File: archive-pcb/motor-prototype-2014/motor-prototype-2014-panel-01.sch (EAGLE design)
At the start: 32 parts, among them J1 JST_VH_2RA, J2 MINIFITJR_HDR_2X2, J3 52852-0870, Q1 SIR438DP, Q2 SIR438DP, Q3 SIR438DP, Q4 SIR438DP, Q5 SIR438DP, Q6 SIR438DP, U1 IRS2336DSOIC28W

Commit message: finalized gerbers for lots of the working designs and moved them to archived directory
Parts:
- added A6-SEL, VSSSEL: (no value), jumper:SJ2W
- added C1, C3: 1 µF, rcl:C-USC0603
- added C10, C9: 1 nF, rcl:C-USC0402
- added C11: 22 µF, 16V, rcl:C-USC0402
- added C12: 100uF, SparkFun-Capacitors:100UF-63V-20%(ELECT)
- added C13: 0.47 µF, 16V, rcl:C-USC0402
- added C14, C15: 0.022 µF, 16V, rcl:C-USC0402
- added C16: 0.1 µF, 50V, rcl:C-USC0603
- added C17, C18: 2.2 µF, 50V, rcl:C-USC0603
- added C19: RC_CAPHE, RoboJackets-Capacitors:RC_CAPHE
- added C2: 2.2 µF, rcl:C-USC0603
- added C20: 0.1uF, adafruit:C-USC0805K
- added C4: 22 nF, rcl:C-USC1206
- added C5: 0.1 µf, rcl:C-USC0603
- added C6, C7, C8: 0.1 µF, rcl:C-USC0402
- added D1, D11, D16, D2, D3, D4, D5, D6, D7, D8, D9: RED, SparkFun-LED:LED-RED0603
- added D10: GRN, SparkFun-LED:LED-RED0603
- added D12, D13, D15: 1N4148WX, RoboJackets-Diodes:1N4148WX
- added D14: DFLS160-7, RoboJackets-Diodes:DFLS160-7
- added D17: P6SMB22A, RoboJackets-Diodes-bad:P6SMB22A
- added D18: MBRX160-TP, RoboJackets-Diodes:DIODE-SOD123
- added F2: FUSE1206, RoboJackets-ICs:FUSE1206
- added F3: FUSE, RoboJackets-Passive:FUSE
- added F4: FUSENANO2, RoboJackets-Passive:FUSENANO2
- added H1, U$4: MOUNTING_HOLE, RoboJackets-Passive:MOUNTING_HOLE
- added IC1: MCP23017, RoboJackets-ICs:MCP23017
- added IC2: DRV8302, RoboJackets-PowerICs:DRV8302
- added IC3: LM25010, RoboJackets-PowerICs:LM25010
- added IC4: MAX6675, adafruit:MAX6675
- added J4: XT-60, RoboJackets-Connectors:XT-60
- added J5: B2PS-VH(LF)(SN), RoboJackets-Connectors:B2PS-VH(LF)(SN)
- added JP1: (no value), SparkFun-Connectors:PINHD-2X10
- added JP2: (no value), SparkFun-Connectors:M03PTH
- added JP3: M02PTH, SparkFun-Connectors:M02PTH
- added JP4: Relay Signal, pinhead:PINHD-1X2/90
- added JP5: 5VIN, pinhead:PINHD-1X2/90
- added JP6: (no value), adafruit:PINHD-1X18
- added L1: SRR1280-101M, RoboJackets-Inductors:SRR1280-101M
- added LED: RGB Led Common Anode, pinhead:PINHD-1X4
- added PL1: (no value), con-molex-2:555X-8V
- added Q7, Q9: BJT-PNP_, RoboJackets-Discrete:BJT-PNP_
- added Q8: MMBT2222A-TP, RoboJackets-Discrete:MMBT2222A-TP
- added R10, R11, R12, R13, R6, R7, R8, R9: 330, SparkFun-Resistors:330OHM1/10W1%(0603)
- added R14, R35, R36, R38: 1 kΩ, rcl:R-US_R0402
- added R15: 150 kΩ, rcl:R-US_R0603
- added R16: 470 kΩ, rcl:R-US_R0402
- added R17: 6.8 kΩ, rcl:R-US_R0402
- added R18, R19: 10 kΩ, rcl:R-US_R0402
- added R20: 1 MΩ, rcl:R-US_R0402
- added R21, R22, R23, R24, R25, R26: 100 Ω, rcl:R-US_R0402
- added R27, R28: 0.002 Ω, rcl:R-US_R1206
- added R29, R30: 1.0 kΩ, rcl:R-US_R0402
- added R31: 1.5 Ω, rcl:R-US_R0402
- added R32: 200 kΩ, rcl:R-US_R0402
- added R33: 680 Ω, rcl:R-US_R0402
- added R34, R37: 100 kΩ, rcl:R-US_R0402
- added R39: 60, resistor:R-US_M0805
- added R40: (no value), resistor:R-US_R0805
- added RST, SERIAL: 22-23-2021, con-molex:22-23-2021
- added S1: SWS003, smd-special:SWS003
- added S2: (no value), RoboJackets-Switches:34EWMSP12MRT
- added S3: 1-1415899-3, RoboJackets-Switches:1-1415899-3
- added SJ1: JUMPER-PAD-3-2OF3_NC_BY_TRACE, SparkFun-Passives:JUMPER-PAD-3-2OF3_NC_BY_TRACE
- added SJ2, SJ3, SJ4, SJ5: JUMPER-PAD-2-NC_BY_TRACE, SparkFun-Passives:JUMPER-PAD-2-NC_BY_TRACE
- added SP1: Speaker, adafruit:SPEAKER/PS12
- added TCOUPLE: 1X2-3.5MM, adafruit:1X2-3.5MM
- added U$2: M18_, SparkFun-Connectors:M18_
- added U$7: ANANO3.3, ArduinoNano:ANANO3.3
- added U2, U3, U4: FDMS3606AS, RoboJackets-Discrete:FDMS3606AS
- added VOLTREG: (no value), RoboJackets-ICs:78MXXS
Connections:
- new net !FAULT!: IC2.!FAULT!, R14.2
- new net +3V3: D9.A, JP1.10, R18.1, S1.5, SJ1.1
- new net +5V: D10.A, D13.C, L1.P$1, R29.2, R31.2, S2.OFF, S3.2
- new net 15: JP6.15
- new net 16: JP6.16
- new net 4.5-18V: PL1-3.S
- new net A0: IC1.A0, R39.1, U$2.18, U$7.A0
- new net A1: IC1.A1, U$2.17
- new net A2: IC1.A2, U$2.16
- new net A5: LED.4, U$7.A5
- new net A6: A6-SEL.2, U$7.A6
- new net A7: LED.1, U$7.A7
- new net ADC_REF: IC2.REF, JP1.13
- new net BACKLIGHT: JP6.10, U$7.D9
- new net BATT+: F2.2, F3.2, F4.2, J4.1, SJ3.2, SJ5.2
- new net BATT_PROTECT_LOGIC: C16.1, C17.1, C18.1, D18.C, IC3.VIN, R32.2
- new net BATT_PROTECT_MOTOR: D17.C, F3.1, F4.1, S3.3, SJ2.2
- new net BIAS: IC2.BIAS, R20.1
- new net BOB: D18.A, F2.1, SJ4.2
- new net BST_A: C6.1, IC2.BST_A
- new net BST_B: C7.1, IC2.BST_B
- new net BST_C: C8.1, IC2.BST_C
- new net CARDDET: A6-SEL.3, JP6.18
- new net CP1: C4.1, IC2.CP1
- new net CP2: C4.2, IC2.CP2
- new net D/C: JP6.8, U$7.D8
- new net DC_CAL: IC2.DC_CAL, JP1.15
- new net DO: IC4.DO, U$7.D4
- new net DTC: IC2.DTC, R15.2, S1.6
- new net GH_A: IC2.GH_A, R26.1
- new net GH_A_F: R26.2, U2.G1
- new net GH_B: IC2.GH_B, R23.1
- new net GH_B_F: R23.2, U3.G1
- new net GH_C: IC2.GH_C, R22.1
- new net GH_C_F: R22.2, U4.G1
- new net GL_A: IC2.GL_A, R25.1
- new net GL_A_F: R25.2, U2.G2
- new net GL_B: IC2.GL_B, R24.1
- new net GL_B_F: R24.2, U3.G2
- new net GL_C: R21.2, U4.G2
- new net GPA0: IC1.GPA0, U$2.12
- new net GPA1: IC1.GPA1, U$2.11
- new net GPA2: IC1.GPA2, U$2.10
- new net GPA3: IC1.GPA3, U$2.9
- new net GPA4: IC1.GPA4, U$2.8
- new net GPA5: IC1.GPA5, U$2.7
- new net GPA6: IC1.GPA6, U$2.6
- new net GPA7: IC1.GPA7, U$2.5
- new net GPB0: IC1.GPB0, R6.2
- new net GPB1: IC1.GPB1, R7.2
- new net GPB2: IC1.GPB2, R8.2
- new net GPB3: IC1.GPB3, R9.2
- new net GPB4: IC1.GPB4, R10.2
- new net GPB5: IC1.GPB5, R11.2
- new net GPB6: IC1.GPB6, R12.2
- new net GPB7: IC1.GPB7, R13.2
- new net HALL-1.1: JP1.6, PL1-1.S
- new net HALL-1.2: JP1.4, PL1-2.S
- new net HALL-1.3: JP1.2, PL1-5.S
- new net INH_A: IC2.INH_A, JP1.1
- new net INH_B: IC2.INH_B, JP1.5
- new net INH_C: IC2.INH_C, JP1.9
- new net INL_A: IC2.INL_A, JP1.3
- new net INL_B: IC2.INL_B, JP1.7
- new net INL_C: IC2.INL_C, JP1.11
- new net INTA: IC1.INTA, U$2.13
- new net INTB: U$2.14
- new net LCDCS: JP6.7, U$7.D10
- new net MISO: JP6.5, U$7.D12
- new net MOSI: JP6.6, U$7.D11
- new net M_PWM: IC2.M_PWM, SJ1.2
- new net N$34: D1.C, R6.1
- new net N$35: D2.C, R7.1
- new net N$36: D3.C, R8.1
- new net N$37: D4.C, R9.1
- new net N$38: D5.C, R10.1
- new net N$39: D6.C, R11.1
- new net N$40: D7.C, R12.1
- new net N$41: D8.C, R13.1
- new net N$45: D9.C, R14.1, R18.2
- new net N$46: IC2.OC_ADJ, R16.2, R17.1, S1.4
- new net N$47: C2.1, IC2.GVDD
- new net N$48: C3.1, IC2.AVDD
- new net N$49: C1.1, IC2.DVDD, R16.1, S1.3
- new net N$50: IC2.EN_BUCK, R19.1
- new net N$51: IC2.GL_C, R21.1
- new net N$52: C15.1, IC3.SS
- new net N$53: C13.1, IC3.VCC
- new net N$54: IC3.FB, R29.1, R30.2
- new net N$55: IC3.RON/SD, R32.1
- new net N$56: C11.1, R31.1
- new net N$57: C14.1, IC3.BST
- new net N$58: C14.2, D14.C, IC3.SW, L1.P$2
- new net N$59: D10.C, R33.2
- new net N$60: D12.C, Q7.B, R34.1
- new net N$61: D11.C, Q7.E
- new net N$62: Q7.C, R34.2, R35.2
- new net N$63: D14.A, IC3.ISEN
- new net N$64: IC2.EN_GATE, S1.2
- new net N$65: D13.A, JP3.2, Q8.C, S3.6
- new net N$66: Q8.B, R36.2
- new net N$67: D16.C, Q9.E
- new net N$68: D15.C, Q9.B, R37.1
- new net N$69: Q9.C, R37.2, R38.2
- new net N$70: JP2.2, R36.1
- new net N$71: JP2.1, S2.C
- new net N$72: D15.A, SJ2.1
- new net N$73: D16.A, SJ3.1
- new net N$74: D12.A, SJ4.1
- new net N$75: D11.A, SJ5.1
- new net N$81: IC4.T+, TCOUPLE.1
- new net N$82: JP4.1, R39.2
- new net N$83: LED.3, R40.2
- new net N$84: A6-SEL.1, LED.2
- new net PHASE-1.1: C6.2, IC2.SH_A, PL1-7.S, U2.PHASE
- new net PHASE-1.2: C7.2, IC2.SH_B, PL1-8.S, U3.PHASE
- new net PHASE-1.3: C8.2, IC2.SH_C, PL1-4.S, U4.PHASE
- new net PWR_DIG: JP1.20, JP2.3
- new net REF: U$7.REF
- new net REGOUT: VOLTREG.OUT, VSSSEL.1
- new net RESET: IC1.!RESET!, JP6.9, U$2.15, U$7.D7
- new net RST: U$7.RST
- new net RST2: RST-2.S, U$7.RST2
- new net RX0: SERIAL-2.S, U$7.RX0
- new net SCL: IC1.SCL, U$2.4
- new net SCLK: JP6.4, U$7.D13
- new net SDA: IC1.SDA, U$2.3
- new net SDCS: JP6.17, U$7.D2
- new net SL_A: C9.1, IC2.SL_A, IC2.SN2, R27.1, U2.SRC
- new net SL_B: C10.1, IC2.SL_B, IC2.SN1, R28.1, U3.SRC
- new net SO1: IC2.SO1, JP1.17
- new net SO2: IC2.SO2, JP1.19
- new net SPK: SP1.+, U$7.D3
- new net TCS: IC4./CS, U$7.D5
- new net TRANSIN: JP5.1, VOLTREG.IN, VSSSEL.3
- new net TSCK: IC4.SCK, U$7.D6
- new net TX1: SERIAL-1.S, U$7.TX1
- new net VDD: C12.+, C19.+, C5.1, D1.A, D2.A, D3.A, D4.A, D5.A, D6.A, D7.A, D8.A, IC1.VDD, IC2.PVDD1, IC2.PVDD2, J5.1, S3.5, U$2.2, U2.DRN, U3.DRN, U4.DRN
- new net VIN: U$7.VIN
- new net VSS: C20.1, IC1.VSS, IC4.VCC, JP6.3, SP1.-, U$2.1, U$4.GND, U$7.3V3
- new net X+: JP6.12, U$7.A2
- new net X-: JP6.14, U$7.A4
- new net Y+: JP6.11, U$7.A1
- new net Y-: JP6.13, U$7.A3
- net GND: now also C1.2, C10.2, C11.2, C12.-, C13.2, C15.2, C16.2, C17.2, C18.2, C19.-, C2.2, C20.2, C3.2, C5.2, C9.2, D17.A, H1.GND, IC2.AGND, IC2.GAIN, IC2.M_OC, IC2.SL_C, IC2.SP1, IC2.SP2, IC2.SS_TR, IC3.RTN, IC3.SGND, IC4.GND, IC4.T-, J4.2, J5.2, JP1.14, JP3.1, JP4.2, JP5.2, JP6.1, PL1-6.S, Q8.E, R15.1, R17.2, R19.2, R20.2, R27.2, R28.2, R30.1, R33.1, R35.1, R38.1, R40.1, RST-1.S, S1.1, S2.ON, SJ1.3, TCOUPLE.2, U$7.GND, U$7.GND2, U4.SRC, VOLTREG.GND
- net VCC: now also JP6.2, U$7.5V, VSSSEL.2
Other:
- note added: "2A"
- note added: "84mA coil current"
- note added: "Backup jumper"
- note added: "Can be used to disconnect fuse LED circuit if needed"
- note added: "Connect lines to disable current protection"
- note added: "Connect lines to set the default dead time"
- note added: "Dead time correction resistor. Dead time of 50ns to 500ns that linear with resistances from 0 to 150 kΩ"
- note added: "Disconnect lines to turn off gate drivers"
- note added: "Jumper for selecting power on/off by switch or by a digital I/O pin"
- note added: "Only connect one fuse at a time. 2 fuses in schematic for comparing them on a physical board"
- note added: "Power output for testing other circuits"
- note added: "This LED is on when the 5V rail is powered"
- note added: "This LED will turn on when a fault is detected (3.3-2.0)/1000 = 1.3 mA"
- note added: "When LOW, must give all 6 PWM inputs. When HIGH, must ONLY give 3 inputs for the HIGH side"
- note added: "~10A"

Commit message: updating gerber files and eagle files for silkscreen layers in motor prototype work
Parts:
- added 916MHZ: ANT-916-CHP-T, RoboJackets-RF:ANT-916-CHP-T
- added IC5: CC1101, RoboJackets-RF:CC1101
- added S4: 94HCB16T, RoboJackets-Switches:94HCB16T
- added S5: JS1300, RoboJackets-Switches:JS1300
- added U$10: NRF24L01ALT2, RoboJackets-RF:NRF24L01ALT2
- added U$11: NRF24L01SMD, RoboJackets-RF:NRF24L01SMD
- added U$12: MPU-6050-1, RoboJackets-Sensors:MPU-6050-1
- added U$9: NRF24L01ALT1, RoboJackets-RF:NRF24L01ALT1
- added U5: LT3757, RoboJackets-ICs:LT3757
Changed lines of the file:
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@@
 <part name="SERIAL" library="con-molex" deviceset="22-23-2021" device="" value=""/>
 <part name="A6-SEL" library="jumper" deviceset="SJ2W" device=""/>
+<part name="916MHZ" library="RoboJackets-RF" deviceset="ANT-916-CHP-?" device="T"/>
+<part name="IC5" library="RoboJackets-RF" deviceset="CC1101" device=""/>
+<part name="U$9" library="RoboJackets-RF" deviceset="NRF24L01" device="ALT1"/>
+<part name="U$10" library="RoboJackets-RF" deviceset="NRF24L01" device="ALT2"/>
+<part name="U$11" library="RoboJackets-RF" deviceset="NRF24L01" device="SMD"/>
+<part name="S4" library="RoboJackets-Switches" deviceset="94HCB16T" device=""/>
+<part name="S5" library="RoboJackets-Switches" deviceset="JS1300" device=""/>
+<part name="U$12" library="RoboJackets-Sensors" deviceset="MPU-6050" device="-1"/>
+<part name="U5" library="RoboJackets-ICs" deviceset="LT3757" device=""/>
 </parts>
 <sheets>
@@
 </nets>
 </sheet>
+<sheet>
+<plain>
+</plain>
+<instances>
+<instance part="916MHZ" gate="G$1" x="17.78" y="35.56"/>
+<instance part="IC5" gate="G$1" x="55.88" y="50.8"/>
+<instance part="U$9" gate="G$1" x="119.38" y="76.2"/>
+<instance part="U$10" gate="G$1" x="193.04" y="78.74"/>
+<instance part="U$11" gate="G$1" x="119.38" y="17.78"/>
+<instance part="S4" gate="G$1" x="7.62" y="7.62"/>
+<instance part="S5" gate=".3" x="-15.24" y="106.68"/>
+<instance part="S5" gate=".1" x="-35.56" y="121.92"/>
+<instance part="S5" gate=".4" x="-35.56" y="88.9"/>
+<instance part="S5" gate=".5" x="10.16" y="88.9"/>
+<instance part="S5" gate=".2" x="10.16" y="119.38"/>
+<instance part="U$12" gate="G$1" x="226.06" y="10.16"/>
+<instance part="U5" gate="G$1" x="185.42" y="-12.7"/>
+</instances>
+<busses>
+</busses>
+<nets>
+</nets>
+</sheet>

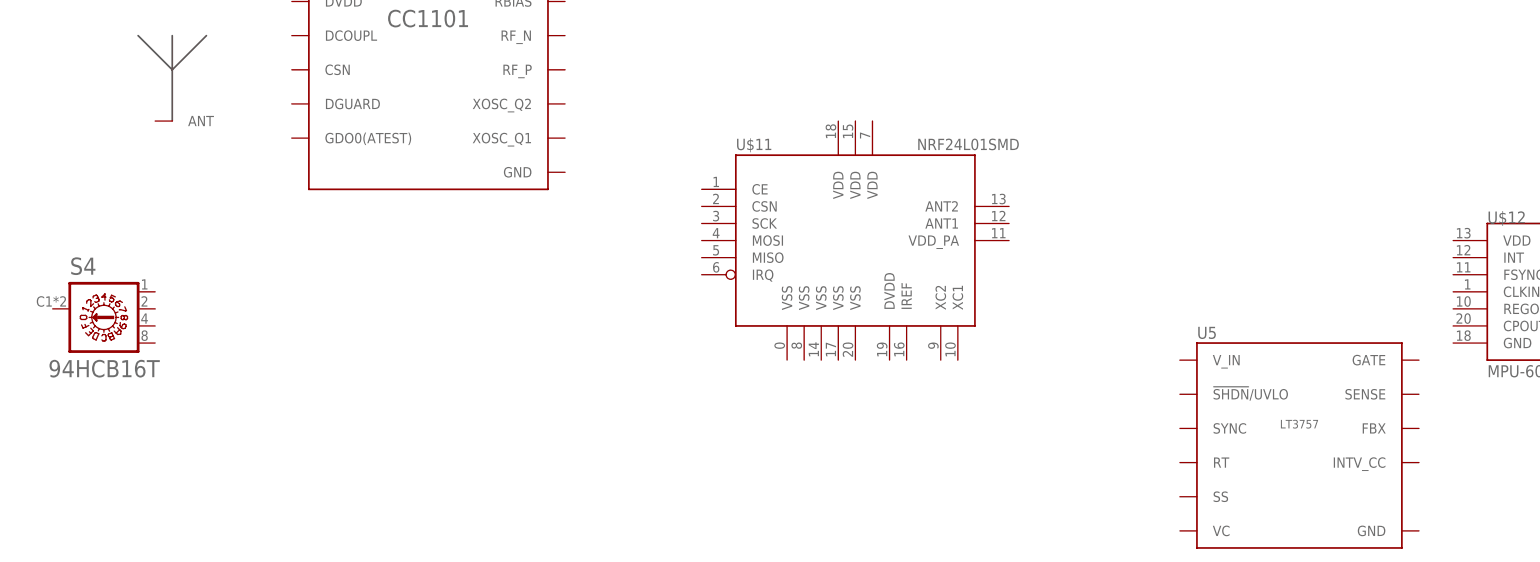
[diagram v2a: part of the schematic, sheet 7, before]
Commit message: adding images, pdfs, and data text files to many previous designs
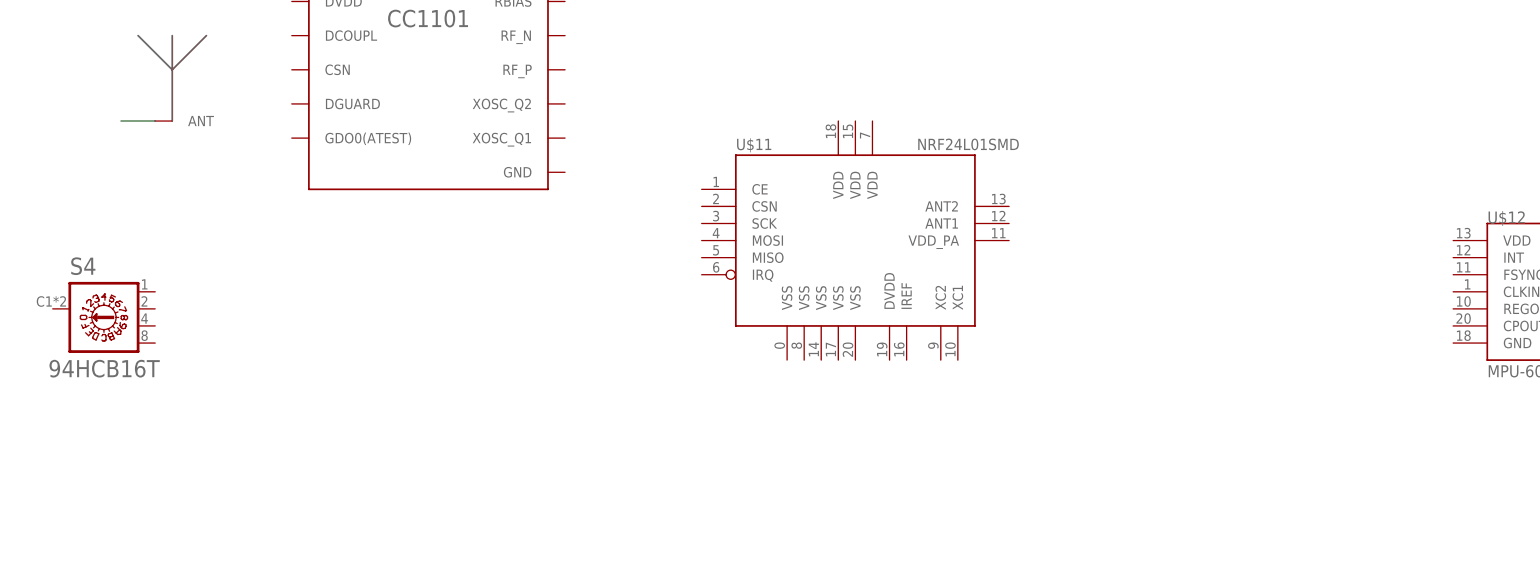
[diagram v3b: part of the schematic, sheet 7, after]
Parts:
- removed U5: LT3757, RoboJackets-ICs:LT3757
- added C21: 100 nF, rcl:C-USC0603
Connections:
- new net ANT_COPPER: 916MHZ.ANT
- net VDD: now also C21.1
- net VSS: now also C21.2
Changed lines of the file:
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@@
 <part name="S5" library="RoboJackets-Switches" deviceset="JS1300" device=""/>
 <part name="U$12" library="RoboJackets-Sensors" deviceset="MPU-6050" device="-1"/>
-<part name="U5" library="RoboJackets-ICs" deviceset="LT3757" device=""/>
+<part name="C21" library="rcl" deviceset="C-US" device="C0603" value="100 nF"/>
 </parts>
 <sheets>
@@
 <instance part="U$2" gate="G$1" x="-96.52" y="45.72"/>
 <instance part="U$4" gate="G$1" x="-45.72" y="20.32"/>
+<instance part="C21" gate="G$1" x="-33.02" y="27.94"/>
 </instances>
 <busses>
@@
 <pinref part="IC1" gate="G$1" pin="VSS"/>
 <label x="2.54" y="33.02" size="1.778" layer="95"/>
-<wire x1="-43.18" y1="20.32" x2="-7.62" y2="20.32" width="0.1524" layer="91"/>
+<wire x1="-43.18" y1="20.32" x2="-33.02" y2="20.32" width="0.1524" layer="91"/>
+<wire x1="-33.02" y1="20.32" x2="-7.62" y2="20.32" width="0.1524" layer="91"/>
 <wire x1="-7.62" y1="20.32" x2="-7.62" y2="33.02" width="0.1524" layer="91"/>
 <wire x1="-7.62" y1="33.02" x2="10.16" y2="33.02" width="0.1524" layer="91"/>
+<pinref part="C21" gate="G$1" pin="2"/>
+<wire x1="-33.02" y1="22.86" x2="-33.02" y2="20.32" width="0.1524" layer="91"/>
+<junction x="-33.02" y="20.32"/>
 </segment>
 <segment>
@@
 <junction x="-48.26" y="93.98"/>
 <junction x="-48.26" y="104.14"/>
-<wire x1="-48.26" y1="25.4" x2="-48.26" y2="38.1" width="0.1524" layer="91"/>
+<wire x1="-48.26" y1="25.4" x2="-48.26" y2="33.02" width="0.1524" layer="91"/>
 <junction x="-48.26" y="38.1"/>
+<pinref part="C21" gate="G$1" pin="1"/>
+<wire x1="-48.26" y1="33.02" x2="-48.26" y2="38.1" width="0.1524" layer="91"/>
+<wire x1="-33.02" y1="30.48" x2="-33.02" y2="33.02" width="0.1524" layer="91"/>
+<wire x1="-33.02" y1="33.02" x2="-48.26" y2="33.02" width="0.1524" layer="91"/>
+<junction x="-48.26" y="33.02"/>
 </segment>
 </net>
@@
 <instance part="S5" gate=".2" x="10.16" y="119.38"/>
 <instance part="U$12" gate="G$1" x="226.06" y="10.16"/>
-<instance part="U5" gate="G$1" x="185.42" y="-12.7"/>
 </instances>
 <busses>
 </busses>
 <nets>
+<net name="ANT_COPPER" class="0">
+<segment>
+<pinref part="916MHZ" gate="G$1" pin="ANT"/>
+<wire x1="15.24" y1="35.56" x2="10.16" y2="35.56" width="0.1524" layer="91"/>
+</segment>
+</net>
 </nets>
 </sheet>
